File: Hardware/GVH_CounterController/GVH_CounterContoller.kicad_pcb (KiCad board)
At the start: 2 copper layers, 82.5 x 88.9 mm, 66 parts, among them J1 Molex Ultra-Fit, J13 Molex Micro-Fit 3pos, J16 Conn_02x08_Odd_Even, J3 WIZnet_J1B1211CCD_RJ45, J4 Molex Micro-Fit 5pos, J5 Molex Micro-Fit 5pos, K1 Relay_DPDT, Q1 MBT2222, SW1 SW_DIP_x02, SW2 SW_MEC_5G, SW3 SW_DIP_x02, U1 Teensy4.1, U10 74LVC2G125DC,125, U11 74LVC2G125DC,125, U12 74LVC2G125DC,125, U14 SN74LVC2G17, U15 AO4882, U2 R-78E5.0-1.0, U3 RT9080-3.3, U4 DS18B20_, U5 74LVC2G125DC,125, U6 74LVC2G125DC,125, U7 74LVC2G125DC,125, U8 74LVC2G125DC,125, U9 74LVC2G125DC,125

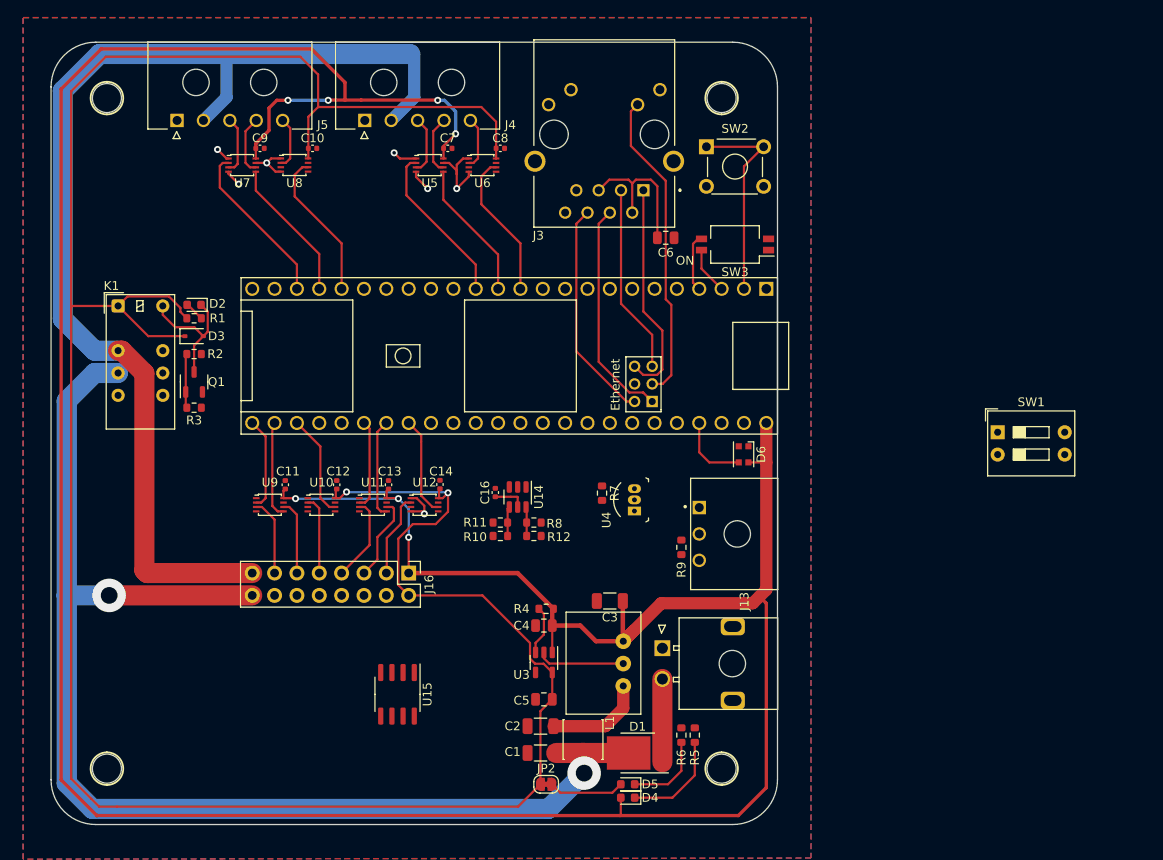
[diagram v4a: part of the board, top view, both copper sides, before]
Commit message: Level shifting redesign complete
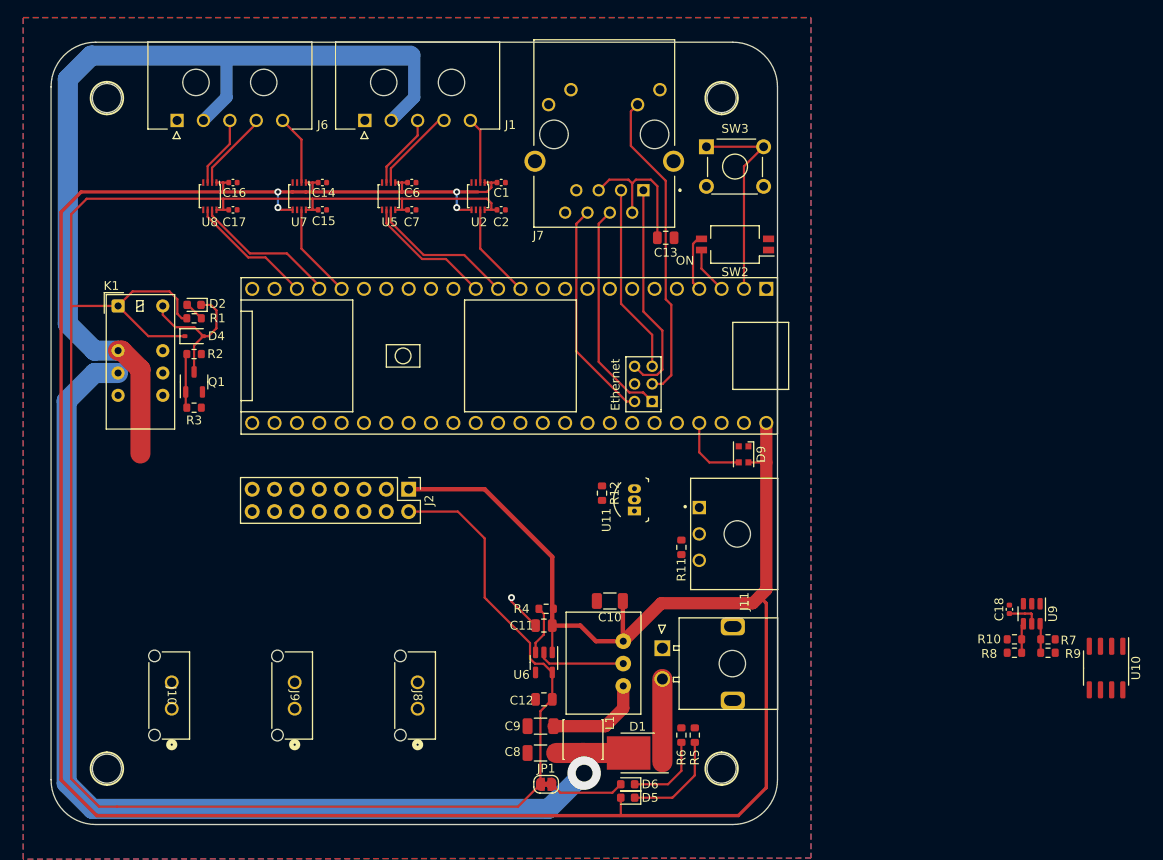
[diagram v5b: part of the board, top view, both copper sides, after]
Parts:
- removed the C10 at (105.9, 62.9)
- removed the C11 at (102.8, 101.1)
- removed the C12 at (108.7, 101.1)
- removed the C13 at (114.6, 101.1)
- removed the C8 at (127.3, 62.9)
- removed the C9 at (99.9, 62.9)
- removed SW1: SW_DIP_x02, Button_Switch_THT:SW_DIP_SPSTx02_Slide_9.78x7.26mm_W7.62mm_P2.54mm
- removed the U10 at (106.9, 103.4)
- removed the U11 at (112.8, 103.4)
- removed U12: 74LVC2G125DC,125, Package_SO:VSSOP-8_2.4x2.1mm_P0.5mm
- removed the U6 at (125.2, 64.8)
- removed the U9 at (101.1, 103.4)
- added C1: 0.1uF, Capacitor_SMD:C_0402_1005Metric, F.Cu at (127.4, 66.8)
- added C15: 0.1uF, Capacitor_SMD:C_0402_1005Metric, F.Cu at (107.0, 69.8)
- added C16: 0.1uF, Capacitor_SMD:C_0402_1005Metric, F.Cu at (96.9, 66.8)
- added C17: 0.1uF, Capacitor_SMD:C_0402_1005Metric, F.Cu at (96.9, 69.8)
- added C2: 0.1uF, Capacitor_SMD:C_0402_1005Metric, F.Cu at (127.4, 69.8)
- added C6: 0.1uF, Capacitor_SMD:C_0402_1005Metric, F.Cu at (117.2, 66.8)
- added J10: Molex Micro-Fit 2pos, 0_connector:MOLEX_MICROFIT-VERT-2POS_436500215, F.Cu at (89.6, 125.0)
- added J8: Molex Micro-Fit 2pos, 0_connector:MOLEX_MICROFIT-VERT-2POS_436500215, F.Cu at (117.6, 125.0)
- added J9: Molex Micro-Fit 2pos, 0_connector:MOLEX_MICROFIT-VERT-2POS_436500215, F.Cu at (103.6, 125.0)
- added U2: SN74LVC2T45, Package_SO:VSSOP-8_2.4x2.1mm_P0.5mm, F.Cu at (124.7, 68.3)
- U5, U7, U8: value 74LVC2G125DC,125 -> SN74LVC2T45DCUR
- moved U10 80.6 mm to (196.1, 121.9)
- moved C18 59.9 mm to (185.1, 115.2)
- moved R7 59.9 mm to (189.5, 120.2)
- moved R9 59.9 mm to (189.5, 118.7)
- moved U9 59.9 mm to (187.6, 115.8)
- moved R10 59.9 mm to (185.7, 118.7)
- moved R8 59.9 mm to (185.7, 120.2)
- moved C14 36.8 mm to (107.0, 66.8), turned to 180 degrees
- moved U8 10.2 mm to (94.2, 68.3), turned to -90 degrees
- moved J2 9.53 mm to (116.8, 101.6)
- moved C7 8.10 mm to (117.2, 69.8), turned to 180 degrees
- moved U7 7.39 mm to (104.4, 68.3), turned to -90 degrees
- moved U5 5.85 mm to (114.6, 68.3), turned to -90 degrees
- renumbered C3 to C10, C4 to C11, C5 to C12, C6 to C13, C16 to C18, C1 to C8, C2 to C9, D3 to D4, D4 to D5, D5 to D6, D6 to D9, J4 to J1, J13 to J11, J16 to J2, J1 to J3, J5 to J6, J3 to J7, JP2 to JP1, R11 to R10, R9 to R11, R7 to R12, R8 to R7, R10 to R8, R12 to R9, SW3 to SW2, SW2 to SW3, U15 to U10, U4 to U11, U1 to U3, U2 to U4, U3 to U6, U14 to U9
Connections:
- net /IO_Level_Shift/CLK_OUT renamed CLK_OUT_0
- net FAN_0 renamed FAN_CTRL_0
- net FAN_1 renamed FAN_CTRL_1
- net Net-(D7-A) renamed FAN_PWR_0
- net Net-(D8-A) renamed FAN_PWR_1
- C14 pad 1: +3.3V -> GND
- C14 pad 2: GND -> +5V
- C7 pad 1: +5V -> GND
- C7 pad 2: GND -> +3.3V
- J1 pad 4: /IO_Level_Shift/LOAD_OUT -> LD_OUT_0
- J1 pad 5: /IO_Level_Shift/SERIAL_IN -> SER_IN_0
- J2 pad 12: GND -> unconnected-(J2-Pin_12-Pad12)
- J2 pad 4: unconnected-(J16-Pin_4-Pad4) -> GND
- J6 pad 3: /IO_Level_Shift1/CLK_OUT -> CLK_OUT_1
- J6 pad 4: /IO_Level_Shift1/LOAD_OUT -> LD_OUT_1
- J6 pad 5: /IO_Level_Shift1/SERIAL_IN -> SER_IN_1
- U3 pad 13: CLK_0 -> LD_0
- U3 pad 14: LOAD_0 -> CLK_0
- U3 pad 21: CLK_1 -> LD_1
- U3 pad 22: LOAD_1 -> CLK_1
- U3 pad 25: LOAD_2 -> unconnected-(U3-33_MCLK2-Pad25)
- U3 pad 26: CLK_2 -> unconnected-(U3-34_RX8-Pad26)
- U3 pad 27: SER_2 -> unconnected-(U3-35_TX8-Pad27)
- U3 pad 35: LOAD_3 -> unconnected-(U3-13_SCK_LED-Pad35)
- U3 pad 36: CLK_3 -> unconnected-(U3-14_A0_TX3_SPDIF_OUT-Pad36)
- U3 pad 37: SER_3 -> unconnected-(U3-15_A1_RX3_SPDIF_IN-Pad37)
- U5 pad 1: GND -> +5V
- U5 pad 2: LOAD_0 -> LD_OUT_0
- U5 pad 5: CLK_0 -> GND
- U5 pad 6: /IO_Level_Shift/LOAD_OUT -> CLK_0
- U5 pad 7: GND -> LD_0
- U5 pad 8: +5V -> +3.3V
- U7 pad 1: GND -> +5V
- U7 pad 2: LOAD_1 -> SER_IN_1
- U7 pad 3: /IO_Level_Shift1/CLK_OUT -> unconnected-(U7-A2-Pad3)
- U7 pad 5: CLK_1 -> +5V
- U7 pad 6: /IO_Level_Shift1/LOAD_OUT -> unconnected-(U7-B2-Pad6)
- U7 pad 7: GND -> SER_1
- U7 pad 8: +5V -> +3.3V
- U8 pad 1: GND -> +5V
- U8 pad 2: /IO_Level_Shift1/SERIAL_IN -> LD_OUT_1
- U8 pad 3: unconnected-(U8-2Y-Pad3) -> CLK_OUT_1
- U8 pad 5: unconnected-(U8-2A-Pad5) -> GND
- U8 pad 6: SER_1 -> CLK_1
- U8 pad 7: unconnected-(U8-~{2OE}-Pad7) -> LD_1
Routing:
- net +3.3V: track 290.4 -> 245.9 mm, vias 2 -> 0
- net +5V: track 365.3 -> 325.6 mm, vias 7 -> 4
- net +12V_ISO: track 131.0 -> 105.1 mm
- net GND: track 37.3 -> 14.2 mm, vias 7 -> 1
- net +12V: track 144.0 -> 122.9 mm, vias 2 -> 1
- net LOAD_1: track 18.7 -> 0.00 mm
- net LOAD_0: track 18.4 -> 0.00 mm
- net LD_0: track 0.00 -> 16.7 mm
- net LD_1: track 0.00 -> 16.5 mm
- net SER_2: track 11.7 -> 0.00 mm
- net SER_3: track 11.3 -> 0.00 mm
- net CLK_3: track 11.3 -> 0.00 mm
- net CLK_2: track 11.2 -> 0.00 mm
- net LOAD_2: track 10.5 -> 0.00 mm
- net LOAD_3: track 10.2 -> 0.00 mm
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
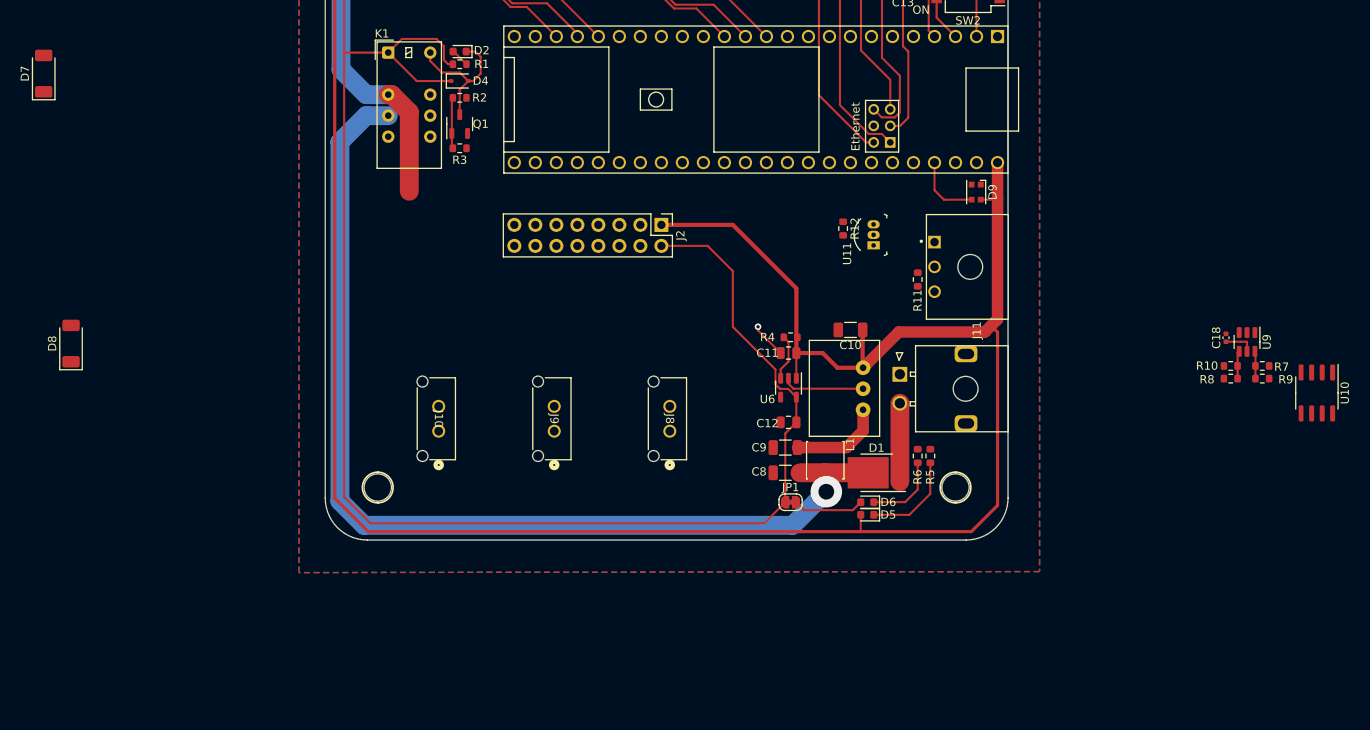
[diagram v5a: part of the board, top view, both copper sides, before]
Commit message: Added Glass fuse and cleaned up fan controller
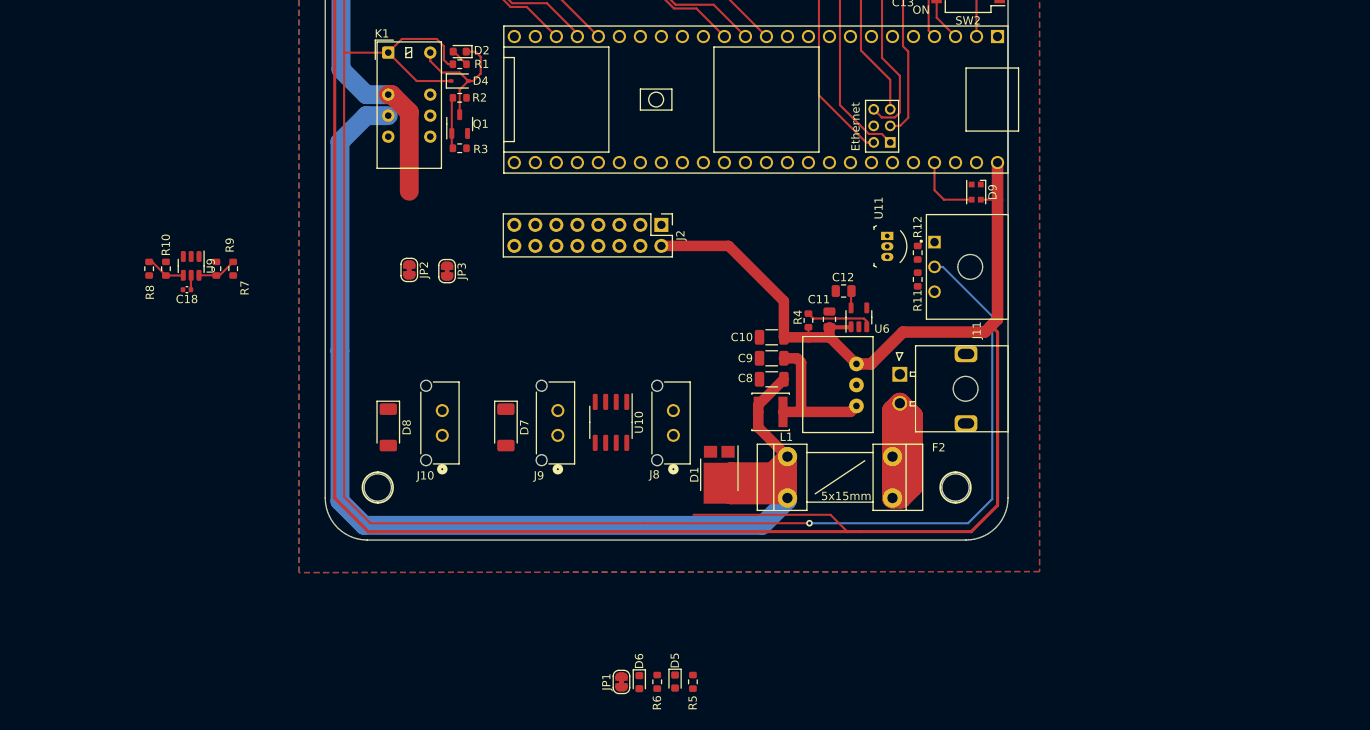
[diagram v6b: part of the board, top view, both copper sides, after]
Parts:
- added F2: Fuse, MeowWolf_Devices:Fuseholder_2AG_5x15mm_Littelfuse_01110501Z, F.Cu at (138.4, 132.1)
- added JP2: SolderJumper_2_Bridged, Jumper:SolderJumper-2_P1.3mm_Bridged_RoundedPad1.0x1.5mm, F.Cu at (86.4, 107.0)
- added JP3: SolderJumper_2_Bridged, Jumper:SolderJumper-2_P1.3mm_Bridged_RoundedPad1.0x1.5mm, F.Cu at (90.9, 107.2)
- moved R8 131.4 mm to (54.9, 106.9), turned to -90 degrees
- moved R10 129.3 mm to (56.9, 106.9), turned to -90 degrees
- moved U9 128.0 mm to (60.0, 106.6)
- moved R9 127.0 mm to (63.0, 106.9), turned to -90 degrees
- moved C18 125.8 mm to (59.5, 109.4), turned to 180 degrees
- moved R7 125.1 mm to (65.1, 106.9), turned to -90 degrees
- moved U10 85.4 mm to (110.7, 125.5)
- moved D7 70.4 mm to (98.0, 126.1), turned to -90 degrees
- moved R6 41.7 mm to (116.3, 156.8)
- moved D8 39.7 mm to (83.8, 126.1), turned to -90 degrees
- moved R5 39.6 mm to (120.7, 156.8)
- moved D6 35.1 mm to (114.2, 156.9), turned to -90 degrees
- moved D5 30.8 mm to (118.5, 156.8), turned to -90 degrees
- moved JP1 29.8 mm to (112.0, 156.9), turned to 90 degrees
- moved D1 19.0 mm to (123.8, 131.8), turned to 90 degrees
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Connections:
- D1 pad 1: Net-(J3-Pin_2) -> GND
- D1 pad 2: Net-(J3-Pin_2) -> GND
- D7 pad 2: FAN_PWR_0 -> FAN_DRAIN_1
- D8 pad 2: FAN_PWR_1 -> FAN_DRAIN_0
- J10 pad 1: FAN_PWR_1 -> FAN_DRAIN_0
- J2 pad 1: +5V -> +3.3V
- J2 pad 2: +3.3V -> +5V
- J8 pad 1: FAN_PWR_0 -> FAN_DRAIN_1
- J9 pad 1: FAN_PWR_1 -> FAN_DRAIN_0
- U10 pad 5: FAN_PWR_1 -> FAN_DRAIN_1
- U10 pad 6: FAN_PWR_1 -> FAN_DRAIN_1
- U10 pad 7: FAN_PWR_0 -> FAN_DRAIN_0
- U10 pad 8: FAN_PWR_0 -> FAN_DRAIN_0
- U9 pad 1: FAN_CTRL_0 -> Net-(JP2-B)
- U9 pad 3: FAN_CTRL_1 -> Net-(JP3-B)
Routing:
- net +12V: track 122.9 -> 158.2 mm, vias 1 -> 0
- net +3.3V: track 245.9 -> 262.6 mm, vias 0 -> 1
- net Net-(J3-Pin_2): track 9.46 -> 25.5 mm
- net GND: track 14.2 -> 0.00 mm, vias 1 -> 0
- net Net-(D5-K): track 11.6 -> 0.00 mm
- net +5V: track 325.6 -> 334.9 mm
- net Net-(D6-K): track 9.18 -> 0.00 mm
- net Net-(D6-A): track 8.63 -> 0.00 mm
- net Net-(U4-IN): track 11.3 -> 17.4 mm
- net Net-(U6-EN): track 5.58 -> 8.09 mm
- net Net-(U9-1Y): track 3.32 -> 4.82 mm
- net Net-(U9-2Y): track 3.37 -> 4.82 mm
